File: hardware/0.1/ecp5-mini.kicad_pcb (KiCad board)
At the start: 4 copper layers, 52 x 27 mm, 102 parts, among them J1 Micro_SD_Card, J2 JTAG, J3 S7 Mini, J4 S7 Mini, J5 USB_C_Receptacle_USB2.0, Q1 BSS138, Q2 BSS138, Q3 BSS138, Q4 BSS138, SW1 SW_Push, U1 ECP5U_12_CABGA256, U2 TLV73325PDBV, U3 TLV62568DBV, U4 USBLC6-2SC6, U5 TLV62568DBV, U6 W25Q128JVSIQ, U7 S27KL0641, X1 DSC6101CI2A-016

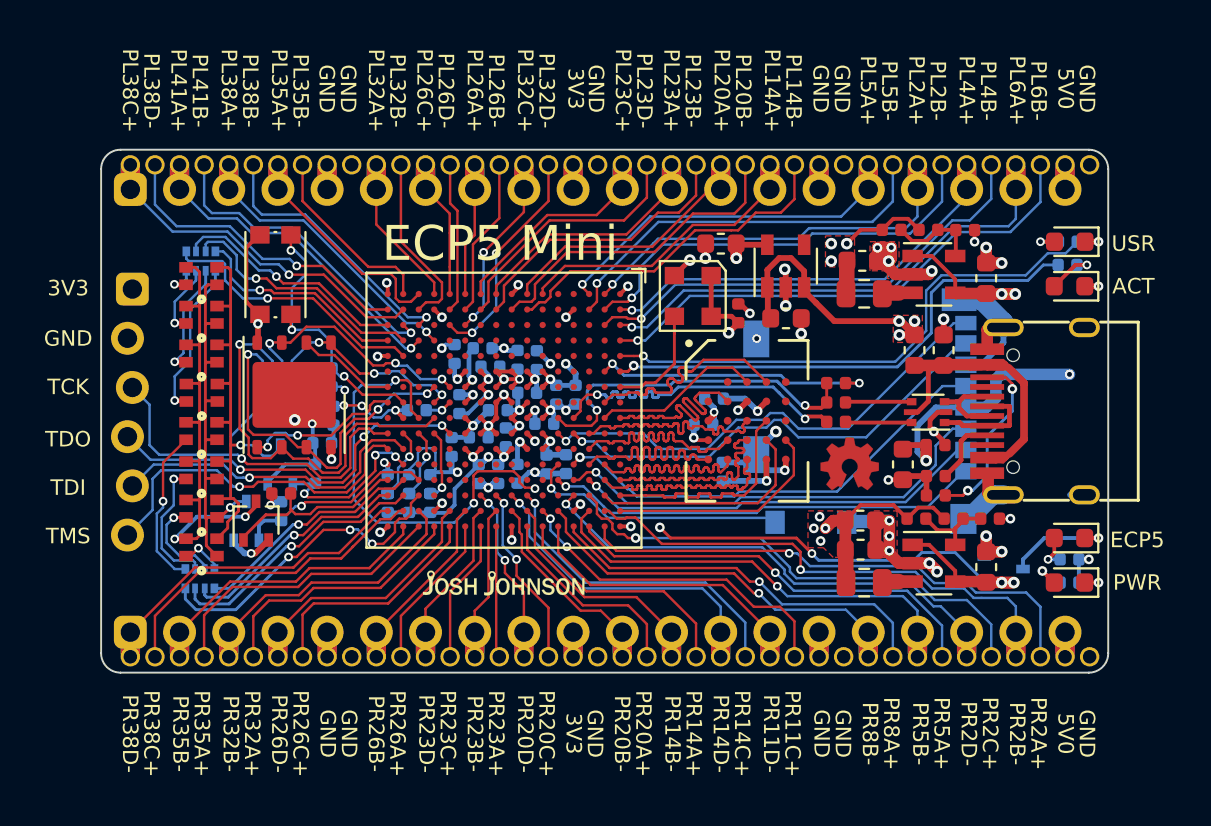
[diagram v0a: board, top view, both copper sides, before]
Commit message: adding silk
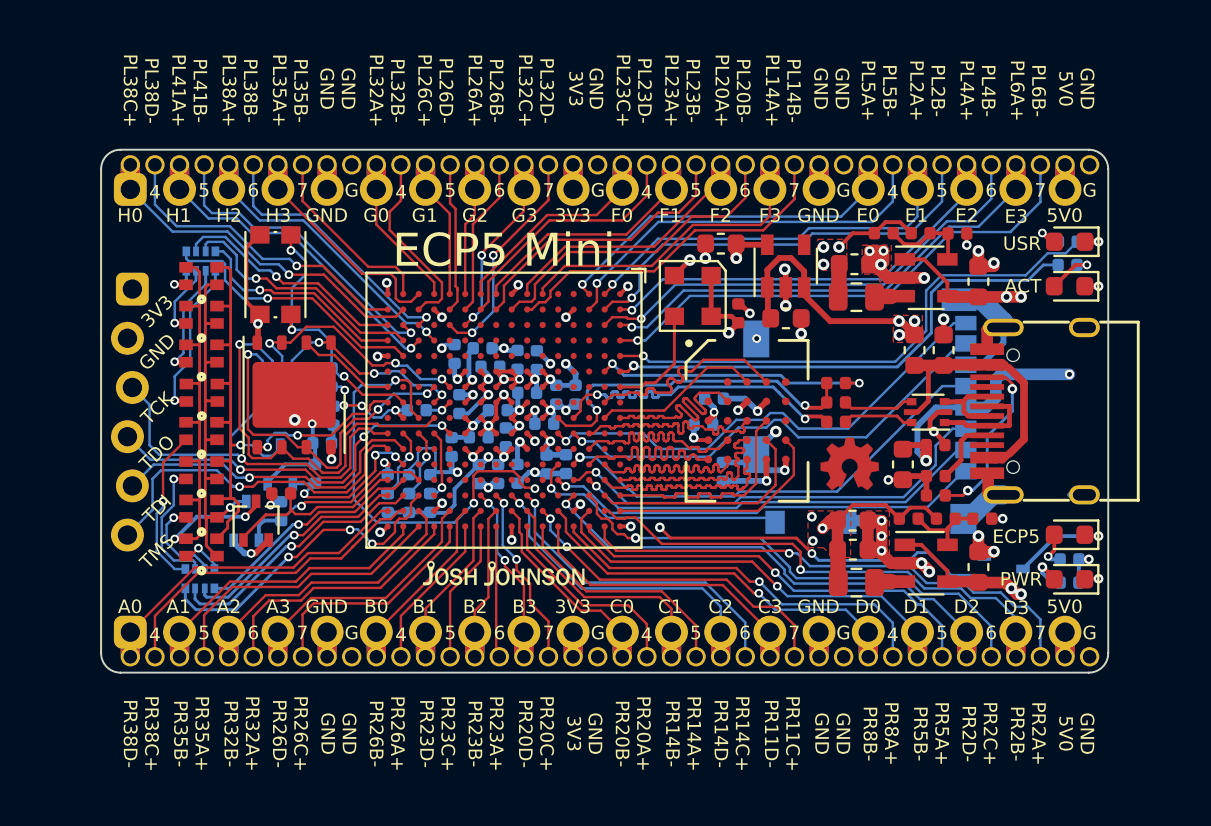
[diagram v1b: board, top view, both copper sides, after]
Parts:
- moved LOGO1 0.50 mm to (117.0, 103.3)
- moved R2 0.44 mm to (140.4, 85.8)
- moved C1 0.44 mm to (141.5, 88.3)
- moved C5 0.44 mm to (135.1, 87.4)
- moved L1 0.44 mm to (135.2, 89.1)
- moved R1 0.44 mm to (138.5, 85.8)
- moved C9 0.44 mm to (136.6, 85.8)
- moved U3 0.44 mm to (138.8, 88.1)
- moved C10 0.40 mm to (135.0, 100.6)
- moved C2 0.40 mm to (141.5, 103.0)
- moved C7 0.40 mm to (135.0, 102.1)
- moved C8 0.40 mm to (137.9, 100.5)
- moved L2 0.40 mm to (135.2, 103.8)
- moved R3 0.40 mm to (139.8, 100.5)
- moved R4 0.40 mm to (141.7, 100.5)
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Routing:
- net GND: track 122.6 -> 120.0 mm
- net +5V: track 73.7 -> 71.6 mm
- net /PORT_E3: track 24.3 -> 23.4 mm
- net /PORT_F3: track 14.1 -> 14.9 mm
- net /PORT_C1: track 10.9 -> 11.6 mm
- net /PORT_D1: track 21.4 -> 20.8 mm
- net +1V1: track 46.3 -> 46.1 mm, vias 8 -> 7
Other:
- board text added: "4"
- board text added: "5"
- board text added: "6"
- board text added: "7"
- board text added: "A0"
- board text added: "A1"
- board text added: "A2"
- board text added: "A3"
- board text added: "B0"
- board text added: "B1"
- board text added: "B2"
- board text added: "B3"
- board text added: "C0"
- board text added: "C1"
- board text added: "C2"
- board text added: "C3"
- board text added: "D0"
- board text added: "D1"
- board text added: "D2"
- board text added: "D3"
- board text added: "E0"
- board text added: "E1"
- board text added: "E2"
- board text added: "E3"
- board text added: "F0"
- board text added: "F1"
- board text added: "F2"
- board text added: "F3"
- board text added: "G"
- board text added: "G0"
- board text added: "G1"
- board text added: "G2"
- board text added: "G3"
- board text added: "H0"
- board text added: "H1"
- board text added: "H2"
- board text added: "H3"

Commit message: change LEDs, optimise parts
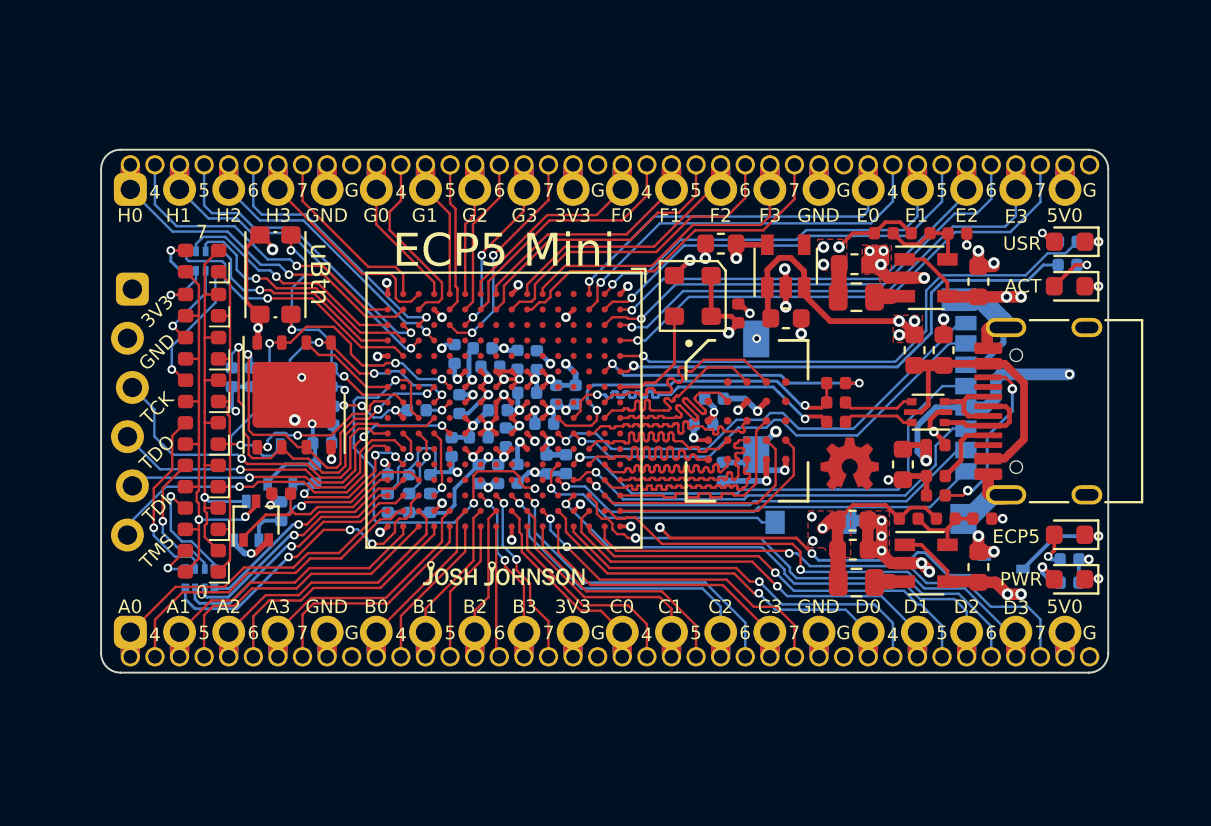
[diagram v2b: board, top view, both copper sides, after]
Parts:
- removed RN1: 10K, Resistor_SMD:R_Array_Convex_4x0402
- added R24: 10K, Resistor_SMD:R_0402_1005Metric, B.Cu at (104.0, 93.2)
- added R26: 10K, Resistor_SMD:R_0402_1005Metric, B.Cu at (105.0, 93.2)
- added R27: 10K, Resistor_SMD:R_0402_1005Metric, B.Cu at (103.0, 93.2)
- added R29: 10K, Resistor_SMD:R_0402_1005Metric, B.Cu at (106.0, 93.2)
- D10, D11, D4, D5, D6, D7, D8, D9: value LED_RGBA -> 2020RGBA; footprint josh-led:LED_0606_E6C0606RGBC3UDA -> josh-led:LED_TRI_2020
- D2: value LED -> PINK
- J5: footprint josh-connectors:USB_C_U262-161N-4BVC11 -> josh-connectors:USB_C_Receptacle_HRO_TYPE-C-31-M-12
- R13, R14, R15, R16, R17, R18: value 1k -> 1K5
- R21, R22, R23, R5: value 1K5 -> 2K2
- SW1: value SW_Push -> KMR2
- moved J5 0.95 mm to (146.1, 95.0)
- moved D11 0.77 mm to (101.4, 87.2), turned to 180 degrees
- moved D4 0.72 mm to (101.4, 102.7), turned to 180 degrees
- moved D5 0.52 mm to (101.4, 100.5), turned to 180 degrees
- moved D10 0.50 mm to (101.4, 89.5), turned to 180 degrees
- moved D6 0.30 mm to (101.4, 98.3), turned to 180 degrees
- moved D9 0.28 mm to (101.4, 91.7), turned to 180 degrees
- moved D7 0.13 mm to (101.4, 96.1), turned to 180 degrees
- moved D8 0.10 mm to (101.4, 93.9), turned to 180 degrees
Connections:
- D10 pad 2: /LEDs/CAT_G -> /LEDs/CAT_B
- D10 pad 3: /LEDs/CAT_B -> Net-(D10-Pad3)
- D10 pad 4: Net-(D10-Pad4) -> /LEDs/CAT_G
- D11 pad 2: /LEDs/CAT_G -> /LEDs/CAT_B
- D11 pad 3: /LEDs/CAT_B -> Net-(D11-Pad3)
- D11 pad 4: Net-(D11-Pad4) -> /LEDs/CAT_G
- D4 pad 2: /LEDs/CAT_G -> /LEDs/CAT_B
- D4 pad 3: /LEDs/CAT_B -> Net-(D4-Pad3)
- D4 pad 4: Net-(D4-Pad4) -> /LEDs/CAT_G
- D5 pad 2: /LEDs/CAT_G -> /LEDs/CAT_B
- D5 pad 3: /LEDs/CAT_B -> Net-(D5-Pad3)
- D5 pad 4: Net-(D5-Pad4) -> /LEDs/CAT_G
- D6 pad 2: /LEDs/CAT_G -> /LEDs/CAT_B
- D6 pad 3: /LEDs/CAT_B -> Net-(D6-Pad3)
- D6 pad 4: Net-(D6-Pad4) -> /LEDs/CAT_G
- D7 pad 2: /LEDs/CAT_G -> /LEDs/CAT_B
- D7 pad 3: /LEDs/CAT_B -> Net-(D7-Pad3)
- D7 pad 4: Net-(D7-Pad4) -> /LEDs/CAT_G
- D8 pad 2: /LEDs/CAT_G -> /LEDs/CAT_B
- D8 pad 3: /LEDs/CAT_B -> Net-(D8-Pad3)
- D8 pad 4: Net-(D8-Pad4) -> /LEDs/CAT_G
- D9 pad 2: /LEDs/CAT_G -> /LEDs/CAT_B
- D9 pad 3: /LEDs/CAT_B -> Net-(D9-Pad3)
- D9 pad 4: Net-(D9-Pad4) -> /LEDs/CAT_G
- RN2 pad 1: Net-(D7-Pad4) -> Net-(D4-Pad3)
- RN2 pad 2: Net-(D6-Pad4) -> Net-(D7-Pad3)
- RN2 pad 3: Net-(D5-Pad4) -> Net-(D6-Pad3)
- RN2 pad 4: Net-(D4-Pad4) -> Net-(D5-Pad3)
- RN2 pad 5: /LED_0 -> /LED_1
- RN2 pad 6: /LED_1 -> /LED_2
- RN2 pad 7: /LED_2 -> /LED_3
- RN2 pad 8: /LED_3 -> /LED_0
- RN3 pad 1: Net-(D8-Pad4) -> Net-(D8-Pad3)
- RN3 pad 2: Net-(D9-Pad4) -> Net-(D9-Pad3)
- RN3 pad 3: Net-(D10-Pad4) -> Net-(D10-Pad3)
- RN3 pad 4: Net-(D11-Pad4) -> Net-(D11-Pad3)
- U1 pad P14: /LED_3 -> /LED_0
- U1 pad R13: /LED_0 -> /LED_1
- U1 pad R14: /LED_2 -> /LED_3
- U1 pad T14: /LED_1 -> /LED_2
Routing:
- net Net-(D7-Pad3): track 0.00 -> 9.75 mm, vias 0 -> 1
- net Net-(D7-Pad4): track 8.23 -> 0.00 mm, vias 1 -> 0
- net Net-(D8-Pad4): track 8.16 -> 0.00 mm, vias 1 -> 0
- net Net-(D6-Pad3): track 0.00 -> 7.08 mm, vias 0 -> 1
- net Net-(D6-Pad4): track 7.00 -> 0.00 mm, vias 1 -> 0
- net Net-(D8-Pad3): track 0.00 -> 6.97 mm, vias 0 -> 1
- net Net-(D5-Pad3): track 0.00 -> 5.97 mm, vias 0 -> 1
- net Net-(D9-Pad4): track 5.96 -> 0.00 mm, vias 1 -> 0
- net Net-(D5-Pad4): track 4.98 -> 0.00 mm, vias 1 -> 0
- net Net-(D9-Pad3): track 0.00 -> 4.47 mm, vias 0 -> 1
- net /LED_0: track 12.1 -> 16.5 mm, vias 1 -> 3
- net GND: track 120.0 -> 115.7 mm, vias 64 -> 66
- net Net-(D10-Pad4): track 3.75 -> 0.00 mm, vias 1 -> 0
- net Net-(D10-Pad3): track 0.00 -> 2.86 mm, vias 0 -> 1
- net /HR_nCS: track 8.74 -> 11.4 mm
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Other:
- board text added: "0"
- board text added: "uBtn"

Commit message: design review done
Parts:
- U4: value USBLC6-2SC6 -> USBLC6-2P6
- U6: value W25Q128JVSIQ -> W25Q128JVPIQ
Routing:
- net GND: track 115.7 -> 119.8 mm, vias 66 -> 68
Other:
- board text added: "2020-09-10"
- board text added: "Rev 0.1"

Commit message: renders
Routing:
- net +3V3: track 65.3 -> 64.5 mm
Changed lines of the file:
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@@
     (pcbplotparams
       (layerselection 0x010fc_ffffffff)
-      (usegerberextensions false)
+      (usegerberextensions true)
       (usegerberattributes false)
-      (usegerberadvancedattributes false)
+      (usegerberadvancedattributes true)
       (creategerberjobfile false)
       (svguseinch false)
@@
       (outputformat 1)
       (mirror false)
-      (drillshape 1)
+      (drillshape 0)
       (scaleselection 1)
-      (outputdirectory "")
+      (outputdirectory "gerbers/")
     )
   )
@@
     (fp_line (start 3 -2.5) (end 3 2.5) (layer "F.Fab") (width 0.1))
     (fp_line (start -3 -1.5) (end -2 -2.5) (layer "F.Fab") (width 0.1))
-    (pad "" smd roundrect (at -0.85 -1.075 270) (size 1.37 1.73) (layers "F.Paste") (roundrect_rratio 0.182482))
-    (pad "" smd roundrect (at -0.85 1.075 270) (size 1.37 1.73) (layers "F.Paste") (roundrect_rratio 0.182482))
-    (pad "" smd roundrect (at 0.85 -1.075 270) (size 1.37 1.73) (layers "F.Paste") (roundrect_rratio 0.182482))
-    (pad "" smd roundrect (at 0.85 1.075 270) (size 1.37 1.73) (layers "F.Paste") (roundrect_rratio 0.182482))
+    (pad "" smd roundrect (at -0.85 -1.075 270) (size 1.37 1.73) (layers "F.Paste") (roundrect_rratio 0.1824817518248175))
+    (pad "" smd roundrect (at -0.85 1.075 270) (size 1.37 1.73) (layers "F.Paste") (roundrect_rratio 0.1824817518248175))
+    (pad "" smd roundrect (at 0.85 -1.075 270) (size 1.37 1.73) (layers "F.Paste") (roundrect_rratio 0.1824817518248175))
+    (pad "" smd roundrect (at 0.85 1.075 270) (size 1.37 1.73) (layers "F.Paste") (roundrect_rratio 0.1824817518248175))
     (pad "1" smd roundrect (at -2.7 -1.905 270) (size 0.75 0.5) (layers "F.Cu" "F.Paste" "F.Mask") (roundrect_rratio 0.25)
       (net 200 "/FPGA Config/CFG_CS") (pinfunction "~CS"))
@@
     (pad "8" smd roundrect (at 2.7 -1.905 270) (size 0.75 0.5) (layers "F.Cu" "F.Paste" "F.Mask") (roundrect_rratio 0.25)
       (net 76 "+3V3") (pinfunction "VCC"))
-    (pad "9" smd roundrect (at 0 0 270) (size 3.4 4.3) (layers "F.Cu" "F.Mask") (roundrect_rratio 0.073529)
+    (pad "9" smd roundrect (at 0 0 270) (size 3.4 4.3) (layers "F.Cu" "F.Mask") (roundrect_rratio 0.07352911764705883)
       (net 61 "GND") (pinfunction "GND"))
     (model "${KISYS3DMOD}/Package_DFN_QFN.3dshapes/DFN-8-1EP_6x5mm_P1.27mm_EP4x4mm.step"
@@
   (segment (start 116.6 92.9) (end 117 93.3) (width 0.2) (layer "F.Cu") (net 76))
   (segment (start 127.7 90.05) (end 127.7 87.95) (width 0.25) (layer "F.Cu") (net 76))
-  (segment (start 117.4 92.9) (end 116.6 92.9) (width 0.2) (layer "F.Cu") (net 76))
   (segment (start 115.4 97.308064) (end 115.399994 97.30807) (width 0.2) (layer "F.Cu") (net 76))
   (segment (start 137.8125 96.7) (end 137.6 96.9125) (width 0.3) (layer "F.Cu") (net 76))
